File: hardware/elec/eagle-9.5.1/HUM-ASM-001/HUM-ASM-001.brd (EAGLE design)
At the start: 99.1 x 99.1 mm, 73 parts, among them J1 B2B-XH-AM(LF)(SN), J2 75869-131LF, J22 75869-131LF, J23 75869-131LF, K1 7-1393239-7, K2 7-1393239-7, Q1 IRLB8721PBF, Q2 IRLB8721PBF, U1 MCP23017-E/SP

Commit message: * Removed unneeded components (Breakout connectors and Jumpers) * Laid 5V and GND planes
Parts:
- removed C3: 100uF, 50V, MG-Eagle_v1:CAP_E-035X080
- removed J24, J25: (no value), MG-Eagle_v1:1X06_NO_SILK
- removed J5, J6: (no value), MG-Eagle_v1:1X14_NO_SILK
- removed JP1, JP2, JP3, JP4, JP5, JP6: CON_JUMPER_PAD-2-NC_BY_TRACE, MG-Eagle_v1:PAD-JUMPER-2-NC_BY_TRACE_YES_SILK
- removed THM-1: 532702B02500G, MG-Eagle_v1:HEATSINK_AAVID_532XX
- moved R4 217.6 mm to (72.4, 45.7), turned to 180 degrees
- moved R3 204.8 mm to (72.4, 49.5), turned to 180 degrees
- moved LED1 196.0 mm to (64.8, 40.6), turned to 90 degrees
- moved R2 192.0 mm to (72.4, 53.3)
- moved J4 183.2 mm to (34.3, 41.9), turned to 90 degrees
- moved JP14 178.9 mm to (43.2, 82.5), turned to 90 degrees
- moved JP11 175.5 mm to (35.6, 82.5), turned to 90 degrees
- moved JP13 173.3 mm to (40.6, 82.5), turned to 90 degrees
- moved J15 170.7 mm to (67.3, 20.3), turned to 270 degrees
- moved R1 168.3 mm to (50.8, 47.0), turned to 90 degrees
- moved JP12 167.6 mm to (38.1, 82.5), turned to 90 degrees
- moved R10 163.4 mm to (45.7, 47.0), turned to 270 degrees
- moved J16 161.9 mm to (67.3, 36.8), turned to 270 degrees
- moved JP10 159.9 mm to (33.0, 82.5), turned to 90 degrees
- moved J3 157.2 mm to (59.7, 31.8), turned to 90 degrees
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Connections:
- removed net N$28: ASM-2.18, J8.11, JP5.1
- removed net N$32: J6.9, U1.20
- removed net N$33: J6.10, U1.19
- removed net N$34: J6.11, JP1.1, U1.18
- removed net N$35: J6.12, JP2.1, U1.17
- removed net N$36: J6.13, JP3.1, U1.16
- removed net N$37: J6.14, JP4.1, U1.15
- removed net N$44: ASM-2.15, J8.14, JP6.1
- net 5V: now also U1.18; no longer C3.+, J24.1, J24.2, J25.1, J25.2, J5.9, JP1.2
- net GND: now also ASM-2.15, ASM-2.18, J8.11, J8.14, U1.15, U1.16, U1.17; no longer C3.-, J24.5, J24.6, J25.5, J25.6, J5.10, JP2.2, JP3.2, JP4.2, JP5.2, JP6.2
- net I2C-SCL: no longer J5.12
- net I2C-SDA: no longer J5.13
- net N$3: no longer J5.1
- net N$4: no longer J5.2
- net N$42: no longer J25.3, J25.4
- net N$9: no longer J24.3, J24.4
- net SFX-0: no longer J6.7
- net SFX-1: no longer J6.6
- net SFX-10: no longer J5.5
- net SFX-2: no longer J6.5
- net SFX-3: no longer J6.4
- net SFX-4: no longer J6.3
- net SFX-5: no longer J6.2
- net SFX-6: no longer J6.1
- net SFX-7: no longer J5.8
- net SFX-8: no longer J5.7
- net SFX-9: no longer J5.6
- net SFX-RST: no longer J6.8
- net SFX-VOL-N: no longer J5.3
- net SFX-VOL-P: no longer J5.4
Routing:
- added copper zone on layer 1, net 5V
- added copper zone on layer 16, net GND
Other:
- outline, holes or cut-outs redrawn

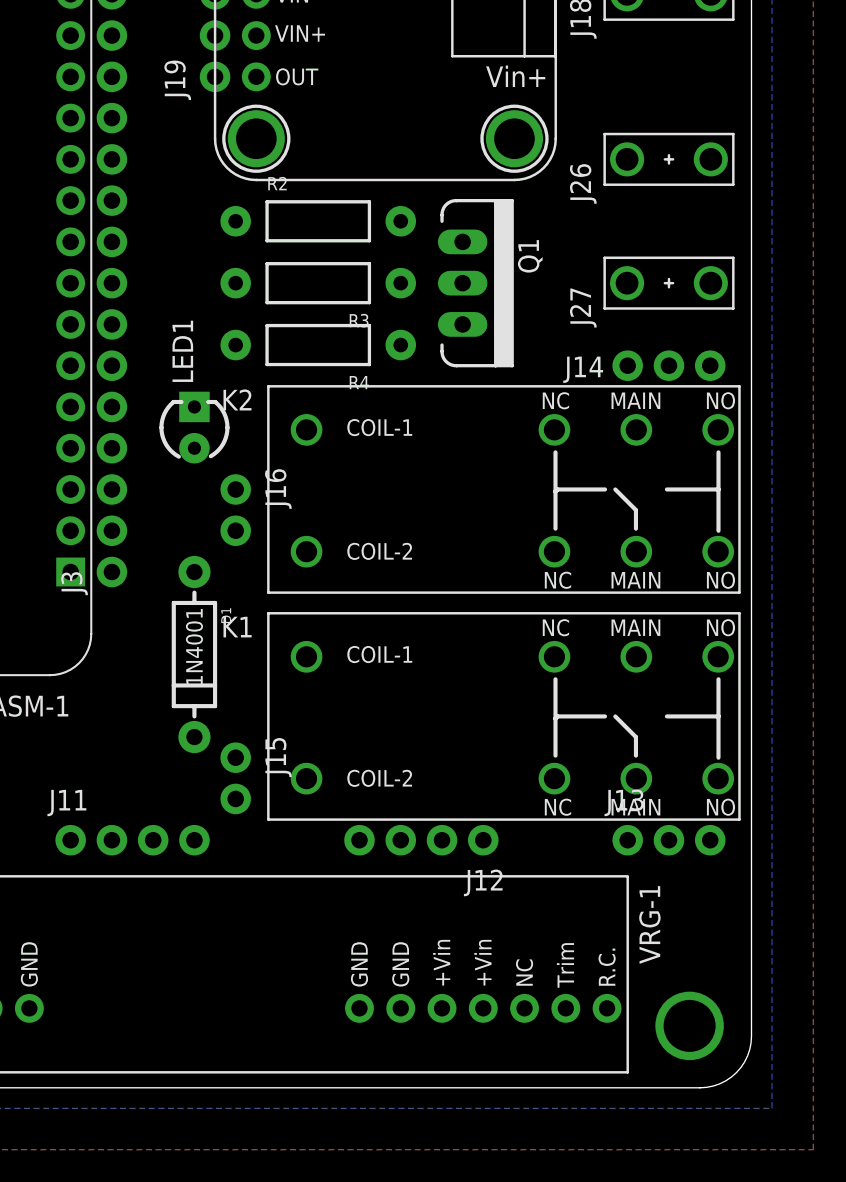
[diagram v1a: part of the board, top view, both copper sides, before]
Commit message: * pre-routed PCB
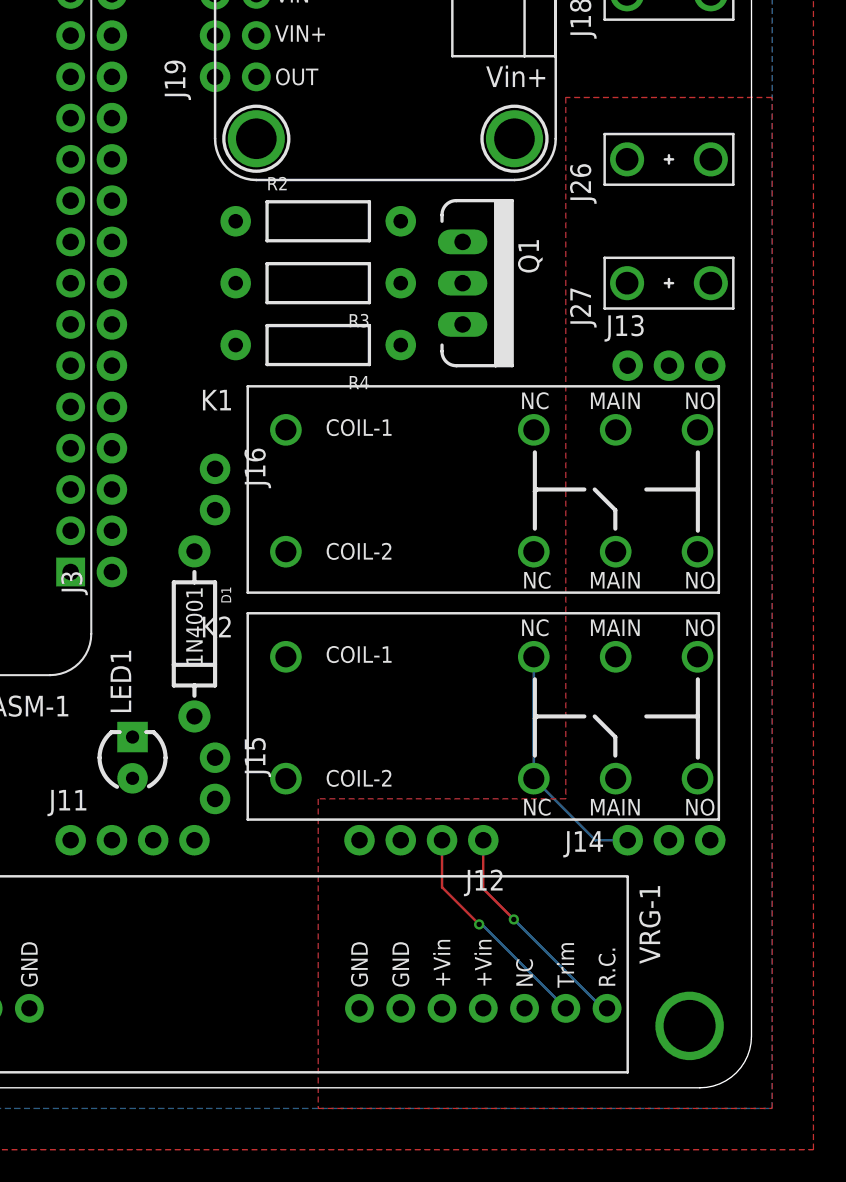
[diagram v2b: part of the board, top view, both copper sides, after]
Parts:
- moved J13 29.2 mm to (91.4, 44.5)
- moved J14 29.2 mm to (91.4, 15.2)
- moved LED1 20.7 mm to (61.0, 20.3)
- moved K1 14.0 mm to (82.5, 36.8)
- moved K2 14.0 mm to (82.5, 22.9)
- moved J16 1.80 mm to (66.0, 38.1)
- moved D1 1.27 mm to (64.8, 27.9)
- moved J15 1.27 mm to (66.0, 20.3)
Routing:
- net K2-NC: track 0.00 -> 14.8 mm
- net N$27: track 0.00 -> 13.7 mm, vias 0 -> 1
- net N$29: track 0.00 -> 13.6 mm, vias 0 -> 1
- added copper zone on layer 1, net 48V

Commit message: * PCB 48V side routed
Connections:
- net K1-NC: no longer K1.NC-2
- net K2-NC: no longer K2.NC-1
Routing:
- net MIST-VIN: track 0.00 -> 92.2 mm
- net N$16: track 0.00 -> 68.4 mm
- net N$10: track 0.00 -> 51.1 mm
- net 48V: track 0.00 -> 32.8 mm
- net N$13: track 0.00 -> 27.3 mm
- net K1-NC: track 0.00 -> 9.06 mm
- net K2-NC: track 14.8 -> 7.35 mm
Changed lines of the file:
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@@
 <contactref element="LED1" pad="K"/>
 <contactref element="R4" pad="P$2"/>
-<wire x1="60.96" y1="21.59" x2="67.31" y2="45.72" width="0" layer="19" extent="1-1"/>
+<wire x1="60.96" y1="21.59" x2="60.96" y2="24.6888" width="0.1524" layer="16"/>
+<wire x1="60.96" y1="24.6888" x2="67.9704" y2="31.6992" width="0.1524" layer="16"/>
+<wire x1="67.9704" y1="31.6992" x2="67.9704" y2="39.3192" width="0.1524" layer="16"/>
+<wire x1="67.31" y1="39.9796" x2="67.31" y2="45.72" width="0.1524" layer="16"/>
+<wire x1="67.9704" y1="39.3192" x2="67.31" y2="39.9796" width="0.1524" layer="16"/>
 </signal>
 <signal name="48V">
@@
 <contactref element="J26" pad="1"/>
 <contactref element="J26" pad="2"/>
-<polygon width="0.1524" layer="1" isolate="0.8128">
+<polygon width="0.3048" layer="1" isolate="0.8128">
 <vertex x="100.33" y="60.96"/>
 <vertex x="87.63" y="60.96"/>
@@
 <vertex x="100.33" y="-1.27"/>
 </polygon>
-<wire x1="91.4019" y1="57.15" x2="82.55" y2="85.09" width="0" layer="19" extent="1-1"/>
+<wire x1="91.4019" y1="57.15" x2="81.0768" y2="67.4751" width="0.889" layer="1"/>
+<wire x1="81.0768" y1="83.6168" x2="82.55" y2="85.09" width="0.889" layer="1"/>
+<wire x1="81.0768" y1="67.4751" x2="81.0768" y2="83.6168" width="0.889" layer="1"/>
 </signal>
 <signal name="N$27">
@@
 <contactref element="D1" pad="A"/>
 <contactref element="R4" pad="P$1"/>
-<wire x1="77.47" y1="45.72" x2="81.28" y2="49.53" width="0" layer="19" extent="1-1"/>
-<wire x1="70.4" y1="33" x2="77.47" y2="45.72" width="0" layer="19" extent="1-1"/>
-<wire x1="66.04" y1="35.56" x2="70.4" y2="33" width="0" layer="19" extent="1-1"/>
-<wire x1="64.77" y1="33.02" x2="66.04" y2="35.56" width="0" layer="19" extent="1-1"/>
-<wire x1="70.4" y1="19.03" x2="70.4" y2="33" width="0" layer="19" extent="1-1"/>
-<wire x1="66.04" y1="17.78" x2="70.4" y2="19.03" width="0" layer="19" extent="1-1"/>
+<wire x1="66.04" y1="17.78" x2="69.15" y2="17.78" width="0.3048" layer="1"/>
+<wire x1="69.15" y1="17.78" x2="70.4" y2="19.03" width="0.3048" layer="1"/>
+<wire x1="66.04" y1="35.56" x2="67.84" y2="35.56" width="0.3048" layer="1"/>
+<wire x1="67.84" y1="35.56" x2="70.4" y2="33" width="0.3048" layer="1"/>
+<wire x1="66.04" y1="35.56" x2="64.77" y2="34.29" width="0.3048" layer="1"/>
+<wire x1="64.77" y1="34.29" x2="64.77" y2="33.02" width="0.3048" layer="1"/>
+<wire x1="70.4" y1="19.03" x2="72.8472" y2="21.4772" width="0.3048" layer="16"/>
+<wire x1="72.8472" y1="30.5528" x2="70.4" y2="33" width="0.3048" layer="16"/>
+<wire x1="72.8472" y1="21.4772" x2="72.8472" y2="30.5528" width="0.3048" layer="16"/>
+<wire x1="81.28" y1="49.53" x2="80.01" y2="49.53" width="0.3048" layer="1"/>
+<wire x1="77.47" y1="46.99" x2="77.47" y2="45.72" width="0.3048" layer="1"/>
+<wire x1="80.01" y1="49.53" x2="77.47" y2="46.99" width="0.3048" layer="1"/>
+<wire x1="77.47" y1="45.72" x2="77.47" y2="40.07" width="0.3048" layer="1"/>
+<wire x1="77.47" y1="40.07" x2="70.4" y2="33" width="0.3048" layer="1"/>
 </signal>
 <signal name="K2-NC">
-<contactref element="K2" pad="NC-1"/>
 <contactref element="K2" pad="NC-2"/>
 <contactref element="J14" pad="1"/>
-<wire x1="91.44" y1="15.24" x2="89.45" y2="15.24" width="0.1524" layer="16"/>
-<wire x1="89.45" y1="15.24" x2="85.66" y2="19.03" width="0.1524" layer="16"/>
-<wire x1="85.66" y1="19.03" x2="85.66" y2="26.53" width="0.1524" layer="16"/>
+<wire x1="91.44" y1="15.24" x2="89.45" y2="15.24" width="0.889" layer="16"/>
+<wire x1="89.45" y1="15.24" x2="85.66" y2="19.03" width="0.889" layer="16"/>
 </signal>
 <signal name="K1-NC">
+<contactref element="J13" pad="1"/>
 <contactref element="K1" pad="NC-1"/>
-<contactref element="K1" pad="NC-2"/>
-<contactref element="J13" pad="1"/>
-<wire x1="85.66" y1="40.5" x2="91.44" y2="44.45" width="0" layer="19" extent="1-1"/>
-<wire x1="85.66" y1="33" x2="85.66" y2="40.5" width="0" layer="19" extent="1-1"/>
+<wire x1="91.44" y1="44.45" x2="86.8172" y2="44.45" width="0.889" layer="16"/>
+<wire x1="86.8172" y1="44.45" x2="85.6488" y2="43.2816" width="0.889" layer="16"/>
+<wire x1="85.6488" y1="43.2816" x2="85.6488" y2="40.5112" width="0.889" layer="16"/>
+<wire x1="85.6488" y1="40.5112" x2="85.66" y2="40.5" width="0.889" layer="16"/>
 </signal>
 <signal name="MIST-VIN">
@@
 <contactref element="J19" pad="3"/>
 <contactref element="ASM-4" pad="3"/>
-<wire x1="91.4019" y1="74.93" x2="96.5581" y2="74.93" width="0" layer="19" extent="1-1"/>
-<wire x1="68.58" y1="67.31" x2="91.4019" y2="74.93" width="0" layer="19" extent="1-1"/>
-<wire x1="66.04" y1="67.31" x2="68.58" y2="67.31" width="0" layer="19" extent="1-1"/>
-<wire x1="96.52" y1="44.45" x2="96.5581" y2="74.93" width="0" layer="19" extent="1-1"/>
-<wire x1="95.74" y1="40.5" x2="96.52" y2="44.45" width="0" layer="19" extent="1-1"/>
-<wire x1="95.74" y1="33" x2="95.74" y2="40.5" width="0" layer="19" extent="1-1"/>
-<wire x1="96.52" y1="15.24" x2="95.74" y2="33" width="0" layer="19" extent="1-1"/>
+<wire x1="96.52" y1="44.45" x2="93.8784" y2="47.0916" width="0.889" layer="16"/>
+<wire x1="93.8784" y1="72.2503" x2="96.5581" y2="74.93" width="0.889" layer="16"/>
+<wire x1="93.8784" y1="47.0916" x2="93.8784" y2="72.2503" width="0.889" layer="16"/>
+<wire x1="96.52" y1="44.45" x2="96.52" y2="41.28" width="0.889" layer="16"/>
+<wire x1="96.52" y1="41.28" x2="95.74" y2="40.5" width="0.889" layer="16"/>
+<wire x1="95.74" y1="33" x2="95.74" y2="40.5" width="0.889" layer="16"/>
+<wire x1="66.04" y1="67.31" x2="68.58" y2="67.31" width="0.889" layer="16"/>
+<wire x1="68.58" y1="67.31" x2="83.7819" y2="67.31" width="0.889" layer="16"/>
+<wire x1="83.7819" y1="67.31" x2="91.4019" y2="74.93" width="0.889" layer="16"/>
+<wire x1="96.52" y1="15.24" x2="97.8408" y2="16.5608" width="0.889" layer="16"/>
+<wire x1="97.8408" y1="30.8992" x2="95.74" y2="33" width="0.889" layer="16"/>
+<wire x1="97.8408" y1="16.5608" x2="97.8408" y2="30.8992" width="0.889" layer="16"/>
+<wire x1="96.5581" y1="74.93" x2="91.4019" y2="74.93" width="0" layer="19" extent="1-1"/>
 </signal>
 <signal name="N$16">
@@
 <contactref element="K2" pad="NO-1"/>
 <contactref element="K2" pad="NO-2"/>
-<wire x1="66.04" y1="64.77" x2="68.58" y2="64.77" width="0" layer="19" extent="1-1"/>
-<wire x1="95.74" y1="26.53" x2="68.58" y2="64.77" width="0" layer="19" extent="1-1"/>
-<wire x1="95.74" y1="19.03" x2="95.74" y2="26.53" width="0" layer="19" extent="1-1"/>
+<wire x1="95.74" y1="26.53" x2="92.3996" y2="29.8704" width="0.889" layer="16"/>
+<wire x1="66.04" y1="64.77" x2="68.58" y2="64.77" width="0.889" layer="16"/>
+<wire x1="84.4296" y1="29.8704" x2="82.6008" y2="31.6992" width="0.889" layer="16"/>
+<wire x1="82.6008" y1="31.6992" x2="82.6008" y2="44.196" width="0.889" layer="16"/>
+<wire x1="82.6008" y1="44.196" x2="84.7344" y2="46.3296" width="0.889" layer="16"/>
+<wire x1="84.7344" y1="46.3296" x2="84.7344" y2="52.7304" width="0.889" layer="16"/>
+<wire x1="84.7344" y1="52.7304" x2="72.6948" y2="64.77" width="0.889" layer="16"/>
+<wire x1="92.3996" y1="29.8704" x2="84.4296" y2="29.8704" width="0.889" layer="16"/>
+<wire x1="72.6948" y1="64.77" x2="68.58" y2="64.77" width="0.889" layer="16"/>
+<wire x1="95.74" y1="19.03" x2="95.74" y2="26.53" width="0.889" layer="16"/>
 </signal>
 <signal name="24V">

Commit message: * PCB Route complete
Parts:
- moved JP7 0.23 mm to (17.9, 78.5), turned to 0 degrees
- moved JP8 0.14 mm to (17.9, 81.2), turned to 0 degrees
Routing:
- net I2C-SDA: track 0.00 -> 73.6 mm, vias 0 -> 2
- net I2C-SCL: track 0.00 -> 69.2 mm
- net ENCODER-SW: track 0.00 -> 52.4 mm
- net N$9: track 0.00 -> 50.6 mm
- net SFX-ROUT: track 0.00 -> 48.0 mm
- net N$42: track 0.00 -> 42.6 mm
- net !AMP-SHDN: track 0.00 -> 42.1 mm
- net ENCODER-A: track 0.00 -> 38.9 mm
- net MIST-CTRL: track 0.00 -> 37.8 mm
- net SFX-LOUT: track 0.00 -> 36.7 mm
- net 24V: track 0.00 -> 32.5 mm
- net ENCODER-B: track 0.00 -> 30.2 mm
- net FAN-CTRL: track 0.00 -> 28.6 mm, vias 0 -> 1
- net CRNT-MON: track 0.00 -> 28.3 mm
- net SFX-9: track 0.00 -> 22.1 mm
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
